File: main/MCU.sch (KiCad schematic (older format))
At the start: 23 parts, among them J4 GPIO breakout, J5 MCU_debug, U4 EFM32GG12B810F1024GQ64, Y1 48MHz

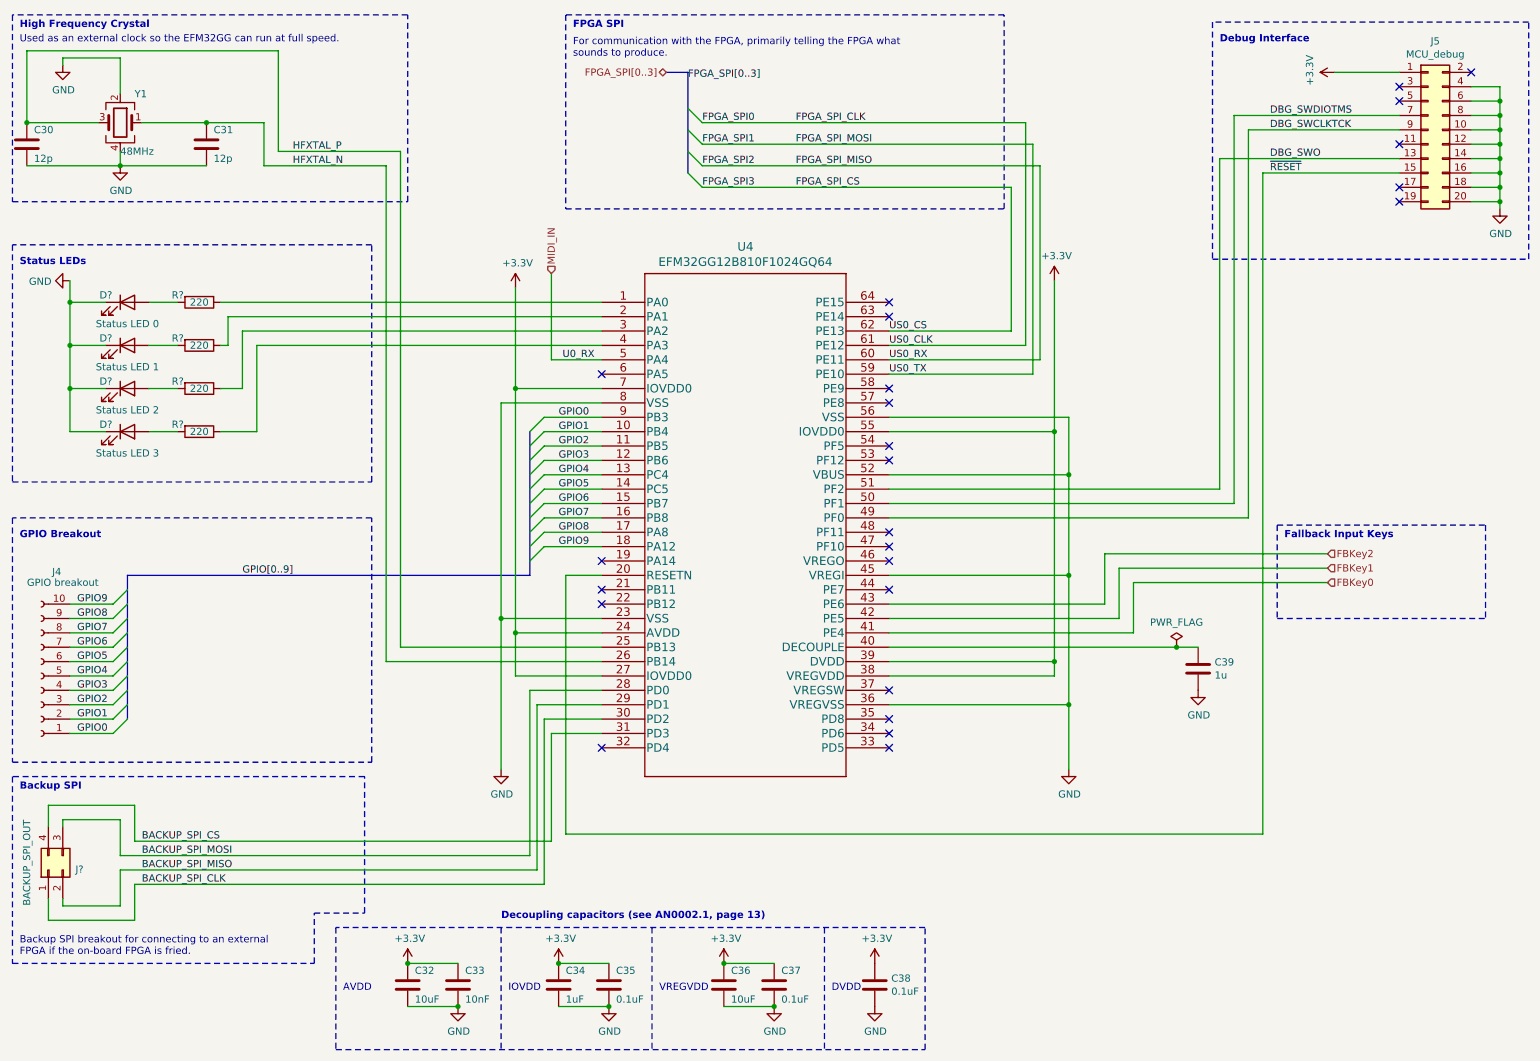
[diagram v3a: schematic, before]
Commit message: Be consistent with capacitor values (always use F)
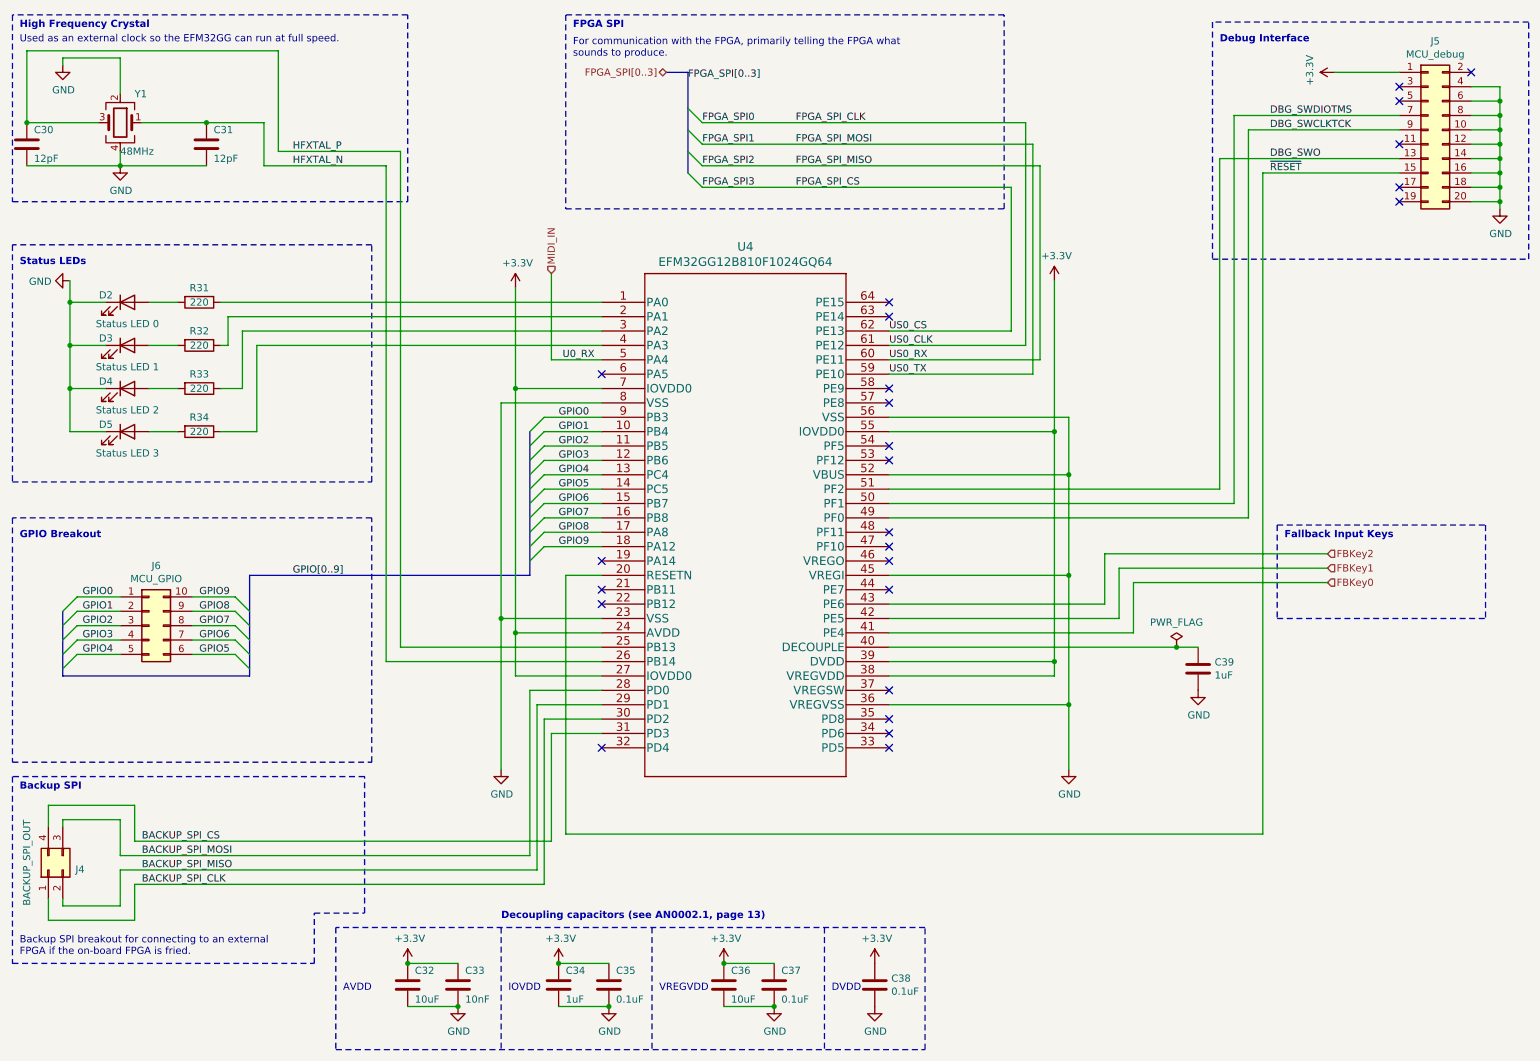
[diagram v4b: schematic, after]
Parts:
- removed J4: GPIO breakout, symbol Connector:Conn_01x10_Female
- added J6: MCU_GPIO, symbol Connector_Generic:Conn_02x05_Counter_Clockwise
- C30, C31: value 12p -> 12pF
- C39: value 1u -> 1uF
- gave numbers to parts that had none: 9
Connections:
- net GPIO0: now also J6.1 (Pin_1)
- net GPIO1: now also J6.2 (Pin_2)
- net GPIO2: now also J6.3 (Pin_3)
- net GPIO3: now also J6.4 (Pin_4)
- net GPIO4: now also J6.5 (Pin_5)
- net GPIO5: now also J6.6 (Pin_6)
- net GPIO6: now also J6.7 (Pin_7)
- net GPIO7: now also J6.8 (Pin_8)
- net GPIO8: now also J6.9 (Pin_9)
- net GPIO9: now also J6.10 (Pin_10)
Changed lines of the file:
@@
 P 650 1450
 F 0 "C30" H 700 1550 50  0000 L CNN
-F 1 "12p" H 700 1350 50  0000 L CNN
+F 1 "12pF" H 700 1350 50  0000 L CNN
 F 2 "" H 688 1300 50  0001 C CNN
 F 3 "~" H 650 1450 50  0001 C CNN
@@
 P 1900 1450
 F 0 "C31" H 1950 1550 50  0000 L CNN
-F 1 "12p" H 1950 1350 50  0000 L CNN
+F 1 "12pF" H 1950 1350 50  0000 L CNN
 F 2 "" H 1938 1300 50  0001 C CNN
 F 3 "~" H 1900 1450 50  0001 C CNN
@@
 Text Notes 600  750  0    50   ~ 0
 Used as an external clock so the EFM32GG can run at full speed.
-$Comp
-L Connector:Conn_01x10_Female J4
-U 1 1 6192A3BC
-P 750 5150
-F 0 "J4" H 642 4425 50  0000 C CNN
-F 1 "GPIO breakout" H 600 4500 50  0000 C CNN
-F 2 "" H 750 5150 50  0001 C CNN
-F 3 "~" H 750 5150 50  0001 C CNN
-	1    750  5150
-	-1   0    0    1
-$EndComp
-Wire Wire Line
-	950  4650 1250 4650
-Entry Wire Line
-	1250 4650 1350 4550
-Wire Wire Line
-	950  4750 1250 4750
-Entry Wire Line
-	1250 4750 1350 4650
-Wire Wire Line
-	950  4850 1250 4850
-Entry Wire Line
-	1250 4850 1350 4750
-Wire Wire Line
-	950  4950 1250 4950
-Entry Wire Line
-	1250 4950 1350 4850
-Wire Wire Line
-	950  5050 1250 5050
-Entry Wire Line
-	1250 5050 1350 4950
-Wire Wire Line
-	950  5150 1250 5150
-Entry Wire Line
-	1250 5150 1350 5050
-Wire Wire Line
-	950  5250 1250 5250
-Entry Wire Line
-	1250 5250 1350 5150
-Wire Wire Line
-	950  5350 1250 5350
-Entry Wire Line
-	1250 5350 1350 5250
-Wire Wire Line
-	950  5450 1250 5450
-Entry Wire Line
-	1250 5450 1350 5350
-Entry Wire Line
-	1250 5550 1350 5450
-Text Label 1000 4950 0    50   ~ 0
+Wire Wire Line
+	1800 4600 2100 4600
+Entry Wire Line
+	2200 4700 2100 4600
+Wire Wire Line
+	1800 4700 2100 4700
+Entry Wire Line
+	2200 4800 2100 4700
+Wire Wire Line
+	1800 4800 2100 4800
+Entry Wire Line
+	2200 4900 2100 4800
+Wire Wire Line
+	1800 4900 2100 4900
+Entry Wire Line
+	2200 5000 2100 4900
+Wire Wire Line
+	1800 5000 2100 5000
+Entry Wire Line
+	2100 5000 2200 5100
+Wire Wire Line
+	1300 5000 1000 5000
+Entry Wire Line
+	1000 5000 900  5100
+Wire Wire Line
+	1300 4900 1000 4900
+Entry Wire Line
+	1000 4900 900  5000
+Wire Wire Line
+	1300 4800 1000 4800
+Entry Wire Line
+	1000 4800 900  4900
+Wire Wire Line
+	1300 4700 1000 4700
+Entry Wire Line
+	1000 4700 900  4800
+Entry Wire Line
+	1000 4600 900  4700
+Text Label 1850 4900 0    50   ~ 0
 GPIO6
-Text Label 1000 5050 0    50   ~ 0
+Text Label 1850 5000 0    50   ~ 0
 GPIO5
-Text Label 1000 5150 0    50   ~ 0
+Text Label 1250 5000 2    50   ~ 0
 GPIO4
-Text Label 1000 5250 0    50   ~ 0
+Text Label 1250 4900 2    50   ~ 0
 GPIO3
-Text Label 1000 5350 0    50   ~ 0
+Text Label 1250 4800 2    50   ~ 0
 GPIO2
-Text Label 1000 5450 0    50   ~ 0
+Text Label 1250 4700 2    50   ~ 0
 GPIO1
-Text Label 1000 5550 0    50   ~ 0
+Text Label 1250 4600 2    50   ~ 0
 GPIO0
 Text Label 6000 1300 0    50   ~ 0
@@
 P 8800 5100
 F 0 "C39" H 8915 5146 50  0000 L CNN
-F 1 "1u" H 8915 5055 50  0000 L CNN
+F 1 "1uF" H 8915 5055 50  0000 L CNN
 F 2 "" H 8838 4950 50  0001 C CNN
 F 3 "~" H 8800 5100 50  0001 C CNN
@@
 $EndComp
 Wire Wire Line
-	950  5550 1250 5550
+	1300 4600 1000 4600
 Wire Wire Line
 	7800 3450 7800 2400
@@
 	1400 6600 1400 6850
 $Comp
-L Connector_Generic:Conn_02x02_Counter_Clockwise J?
+L Connector_Generic:Conn_02x02_Counter_Clockwise J4
 U 1 1 617FA2E9
 P 800 6500
-F 0 "J?" V 804 6312 50  0000 R CNN
+F 0 "J4" V 804 6312 50  0000 R CNN
 F 1 "BACKUP_SPI_OUT" H 1150 6650 50  0000 R CNN
 F 2 "" H 800 6500 50  0001 C CNN
@@
 BACKUP_SPI_MOSI
 $Comp
-L Device:LED D?
+L Device:LED D5
 U 1 1 6189B0E4
 P 1350 3450
-F 0 "D?" H 1200 3500 50  0000 C CNN
+F 0 "D5" H 1200 3500 50  0000 C CNN
 F 1 "Status LED 3" H 1350 3300 50  0000 C CNN
 F 2 "" H 1350 3450 50  0001 C CNN
@@
 $EndComp
 $Comp
-L Device:R R?
+L Device:R R34
 U 1 1 6189BBB6
 P 1850 3450
-F 0 "R?" V 1800 3300 50  0000 C CNN
+F 0 "R34" V 1750 3450 50  0000 C CNN
 F 1 "220" V 1850 3450 50  0000 C CNN
 F 2 "" V 1780 3450 50  0001 C CNN
@@
 	1200 3450 950  3450
 $Comp
-L power:GND #PWR?
+L power:GND #PWR0164
 U 1 1 618B3507
 P 950 2400
-F 0 "#PWR?" H 950 2150 50  0001 C CNN
+F 0 "#PWR0164" H 950 2150 50  0001 C CNN
 F 1 "GND" V 955 2272 50  0000 R CNN
 F 2 "" H 950 2400 50  0001 C CNN
@@
 $EndComp
 $Comp
-L Device:LED D?
+L Device:LED D4
 U 1 1 618B492D
 P 1350 3150
-F 0 "D?" H 1200 3200 50  0000 C CNN
+F 0 "D4" H 1200 3200 50  0000 C CNN
 F 1 "Status LED 2" H 1350 3000 50  0000 C CNN
 F 2 "" H 1350 3150 50  0001 C CNN
@@
 $EndComp
 $Comp
-L Device:R R?
+L Device:R R33
 U 1 1 618B4933
 P 1850 3150
-F 0 "R?" V 1800 3000 50  0000 C CNN
+F 0 "R33" V 1750 3150 50  0000 C CNN
 F 1 "220" V 1850 3150 50  0000 C CNN
 F 2 "" V 1780 3150 50  0001 C CNN
@@
 	1200 3150 950  3150
 $Comp
-L Device:LED D?
+L Device:LED D3
 U 1 1 618BB150
 P 1350 2850
-F 0 "D?" H 1200 2900 50  0000 C CNN
+F 0 "D3" H 1200 2900 50  0000 C CNN
 F 1 "Status LED 1" H 1350 2700 50  0000 C CNN
 F 2 "" H 1350 2850 50  0001 C CNN
@@
 $EndComp
 $Comp
-L Device:R R?
+L Device:R R32
 U 1 1 618BB156
 P 1850 2850
-F 0 "R?" V 1800 2700 50  0000 C CNN
+F 0 "R32" V 1750 2850 50  0000 C CNN
 F 1 "220" V 1850 2850 50  0000 C CNN
 F 2 "" V 1780 2850 50  0001 C CNN
@@
 	1200 2850 950  2850
 $Comp
-L Device:LED D?
+L Device:LED D2
 U 1 1 618C9146
 P 1350 2550
-F 0 "D?" H 1200 2600 50  0000 C CNN
+F 0 "D2" H 1200 2600 50  0000 C CNN
 F 1 "Status LED 0" H 1350 2400 50  0000 C CNN
 F 2 "" H 1350 2550 50  0001 C CNN
@@
 $EndComp
 $Comp
-L Device:R R?
+L Device:R R31
 U 1 1 618C914C
 P 1850 2550
-F 0 "R?" V 1800 2400 50  0000 C CNN
+F 0 "R31" V 1750 2550 50  0000 C CNN
 F 1 "220" V 1850 2550 50  0000 C CNN
 F 2 "" V 1780 2550 50  0001 C CNN
@@
 Wire Wire Line
 	4300 2350 4300 2950
-Text Label 1000 4850 0    50   ~ 0
+Text Label 1850 4800 0    50   ~ 0
 GPIO7
-Text Label 1000 4750 0    50   ~ 0
+Text Label 1850 4700 0    50   ~ 0
 GPIO8
-Text Label 1000 4650 0    50   ~ 0
+Text Label 1850 4600 0    50   ~ 0
 GPIO9
-Text Label 2150 4450 0    50   ~ 0
+Text Label 2500 4450 0    50   ~ 0
 GPIO[0..9]
 Wire Wire Line
@@
 GPIO6
 NoConn ~ 4650 4350
-Wire Bus Line
-	1350 4450 4150 4450
 Wire Notes Line
 	550  2150 550  3800
@@
 Text Notes 4450 850  0    50   ~ 0
 For communication with the FPGA, primarily telling the FPGA what\nsounds to produce.
-Wire Bus Line
-	5250 950  5250 1650
-Wire Bus Line
-	4150 3450 4150 4450
-Wire Bus Line
-	1350 4450 1350 5450
 Text Notes 600  5950 0    50   ~ 10
 Backup SPI
 Text Notes 3950 6850 0    50   ~ 10
 Decoupling capacitors (see AN0002.1, page 13)
+$Comp
+L Connector_Generic:Conn_02x05_Counter_Clockwise J6
+U 1 1 6149651E
+P 1500 4800
+F 0 "J6" H 1550 5217 50  0000 C CNN
+F 1 "MCU_GPIO" H 1550 5126 50  0000 C CNN
+F 2 "" H 1500 4800 50  0001 C CNN
+F 3 "~" H 1500 4800 50  0001 C CNN
+	1    1500 4800
+	1    0    0    -1
+$EndComp
+Wire Bus Line
+	900  5150 2200 5150
+Wire Bus Line
+	2200 4450 4150 4450
+Wire Bus Line
+	5250 950  5250 1650
+Wire Bus Line
+	2200 4450 2200 5150
+Wire Bus Line
+	900  4700 900  5150
+Wire Bus Line
+	4150 3450 4150 4450
 $EndSCHEMATC

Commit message: Some tweaks
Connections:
- net external_clock_out: now reaches U4.32 (PD4)
- no-connect marks 25 -> 24
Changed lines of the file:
@@
 encoding utf-8
 Sheet 3 7
-Title ""
-Date ""
-Rev ""
+Title "MIDI Audio Box"
+Date "2021-09-21"
+Rev "v01"
 Comp ""
 Comment1 ""
 Comment2 ""
-Comment3 ""
-Comment4 ""
+Comment3 "Authors: Iver Håkonsen, Halvor Bjørstad"
+Comment4 "TDT4295 Computer Design Project"
 $EndDescr
 Text HLabel 4300 2350 1    50   Input ~ 0
@@
 	4150 5250 4150 6400
 NoConn ~ 6650 5550
-NoConn ~ 4650 5650
 Wire Wire Line
 	4650 5150 4050 5150
@@
 Wire Bus Line
 	2200 4450 4150 4450
+Wire Wire Line
+	4650 5650 4550 5650
+Wire Wire Line
+	4550 5650 4550 6100
+Wire Wire Line
+	4550 6100 5250 6100
 Wire Bus Line
 	5250 950  5250 1650
@@
 Wire Bus Line
 	4150 3450 4150 4450
+Text HLabel 5250 6100 2    50   Output ~ 0
+external_clock_out
 $EndSCHEMATC
